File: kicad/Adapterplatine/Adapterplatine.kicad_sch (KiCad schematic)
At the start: 4 parts, among them X36A1 DE9_Pins, X40 Conn_01x02_Pin, X45 DE9_Pins, X52 Conn_01x05_Pin

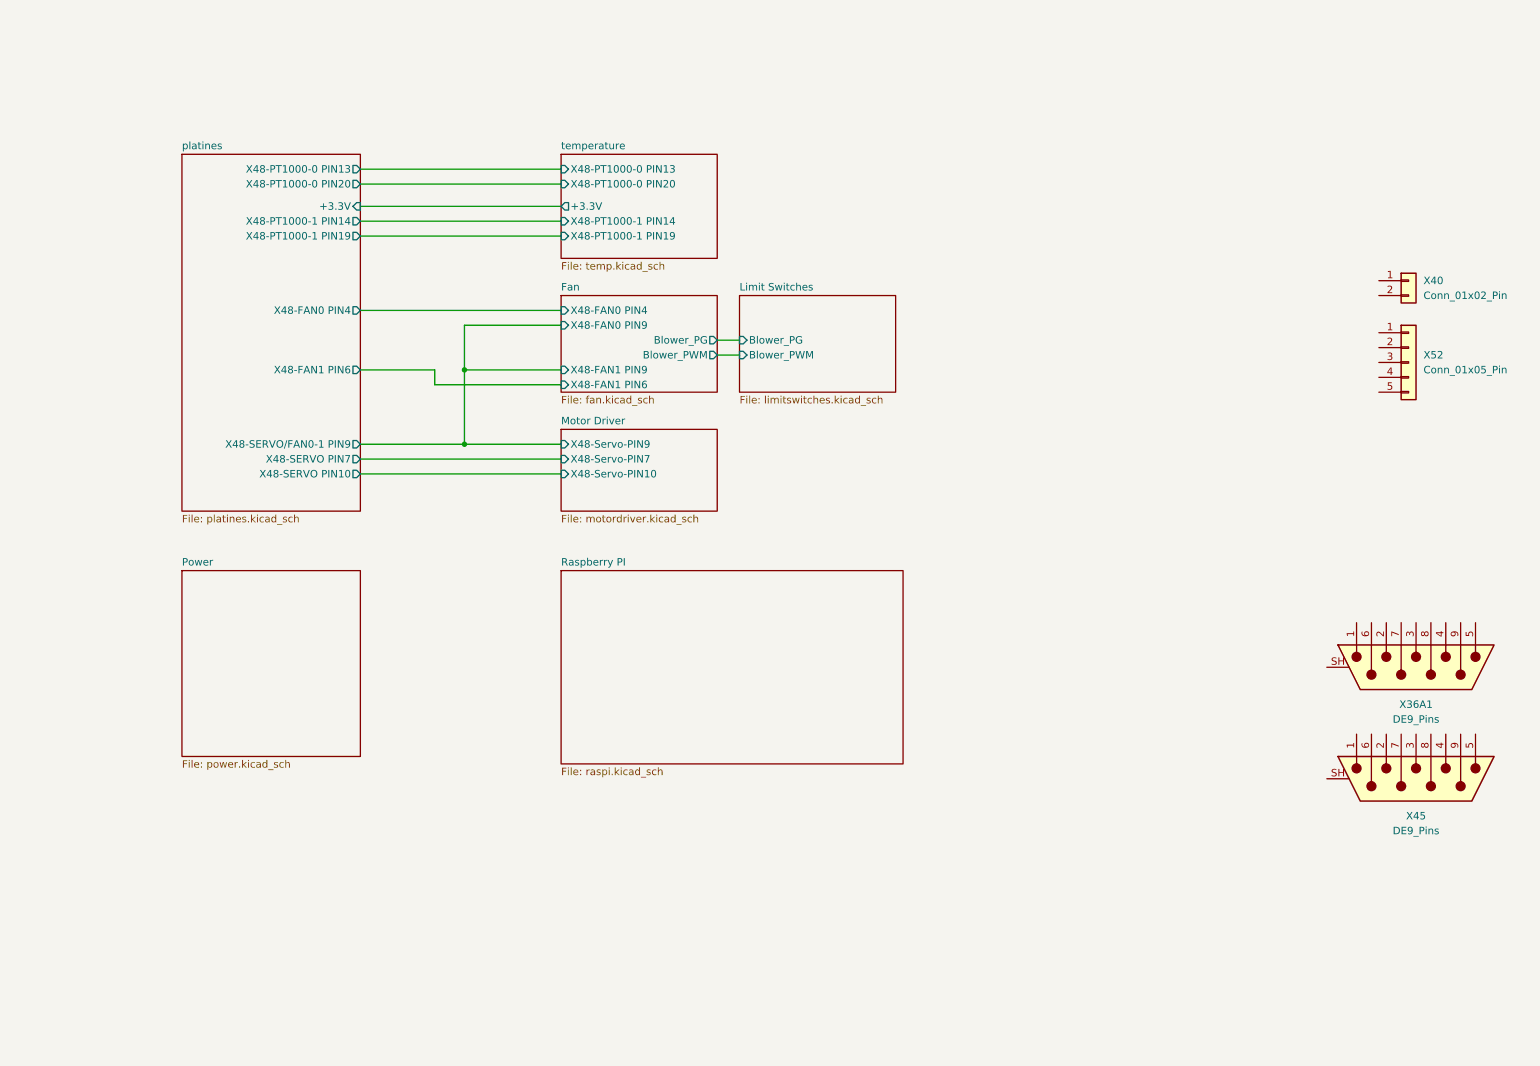
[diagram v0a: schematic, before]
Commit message: Abschlussbericht angefangen/ Adapterplatine ECR DCR
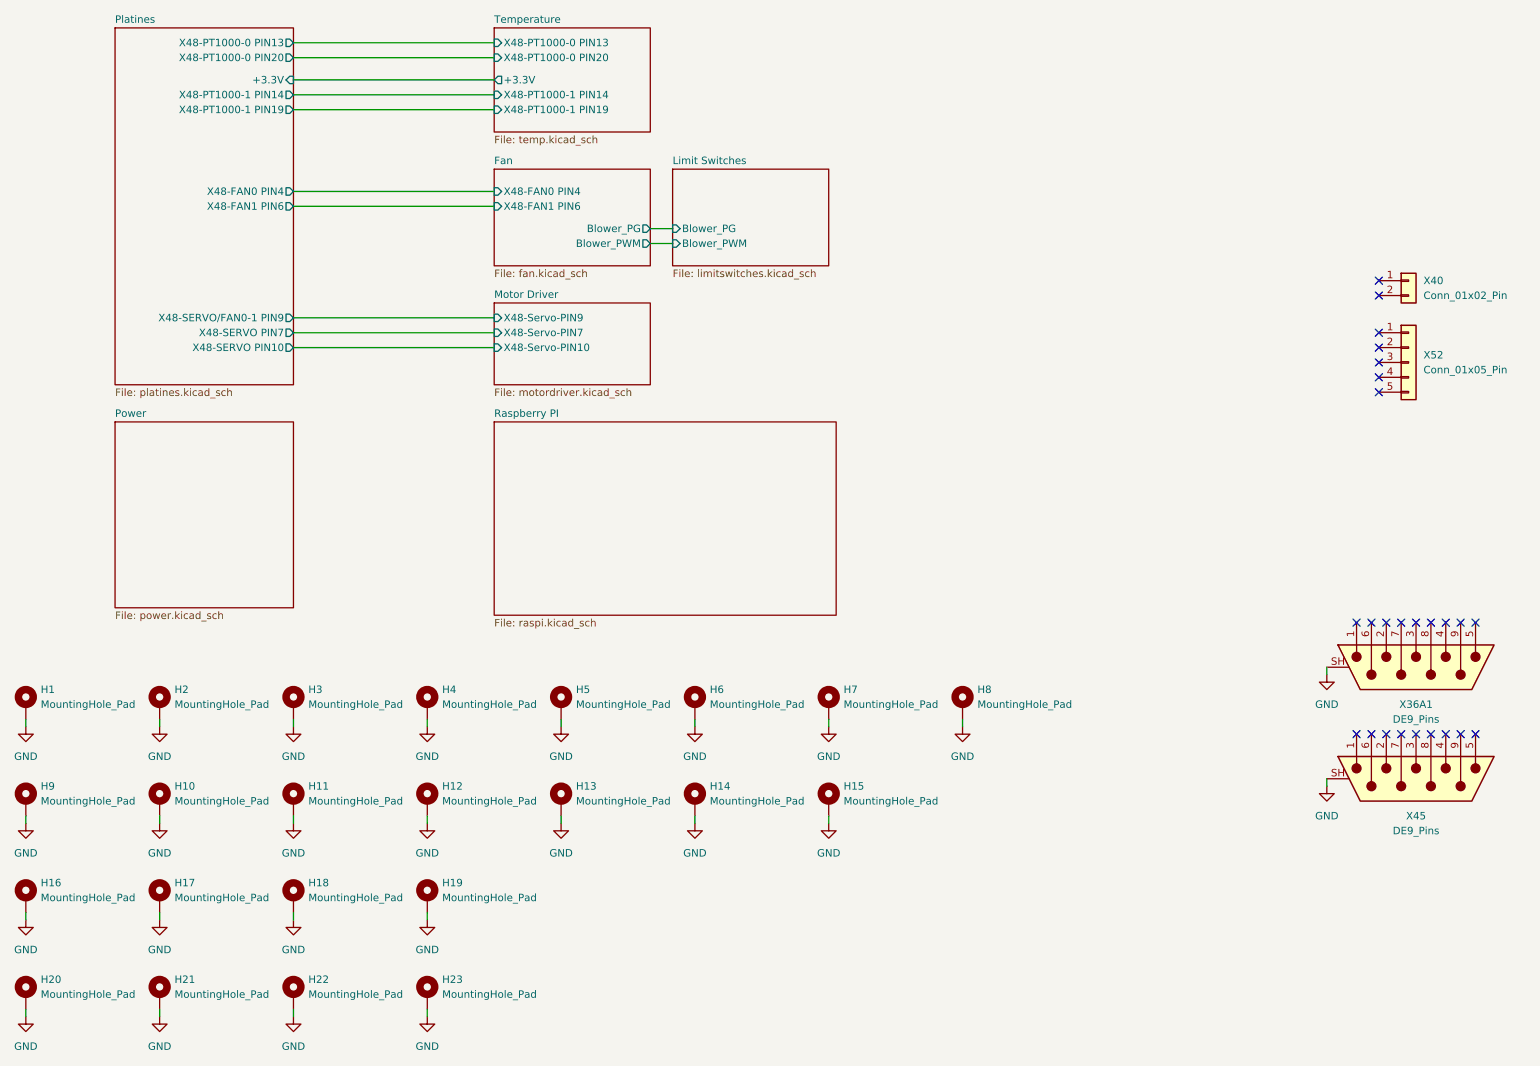
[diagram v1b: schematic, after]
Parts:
- added H1, H10, H11, H12, H13, H14, H15, H2, H3, H4, H5, H6, H7, H8, H9: MountingHole_Pad, MountingHole:MountingHole_3.5mm_Pad, symbol Mechanical:MountingHole_Pad
- added H16, H17, H18, H19, H20, H21, H22, H23: MountingHole_Pad, MountingHole:MountingHole_3.5mm_Pad_Via, symbol Mechanical:MountingHole_Pad
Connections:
- net GND: now reaches X45.SH (PAD)
- net GND: now also X36A1.SH (PAD), H1.1, H10.1, H11.1, H12.1, H13.1, H14.1, H15.1, H16.1, H17.1, H18.1, H19.1, H2.1, H20.1, H21.1, H22.1, H23.1, H3.1, H4.1, H5.1, H6.1, H7.1, H8.1, H9.1
- no-connect marks 0 -> 25
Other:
- sheet platines renamed Platines
- sheet temperature renamed Temperature
- sheet Fan ports: added none; removed X48-FAN0 PIN9, X48-FAN1 PIN9

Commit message: Adapterplatine Version 1.0
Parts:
- H16, H17, H18, H19, H20, H21, H22, H23: footprint MountingHole:MountingHole_3.5mm_Pad_Via -> Platines:MountingHole_3.5mm_Pad_Via_10mm_Aufbau
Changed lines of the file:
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@@
 			)
 		)
-		(property "Footprint" "MountingHole:MountingHole_3.5mm_Pad_Via"
+		(property "Footprint" "Platines:MountingHole_3.5mm_Pad_Via_10mm_Aufbau"
 			(at 40.64 186.69 0)
 			(hide yes)
@@
 			)
 		)
-		(property "Footprint" "MountingHole:MountingHole_3.5mm_Pad_Via"
+		(property "Footprint" "Platines:MountingHole_3.5mm_Pad_Via_10mm_Aufbau"
 			(at 63.5 186.69 0)
 			(hide yes)
@@
 			)
 		)
-		(property "Footprint" "MountingHole:MountingHole_3.5mm_Pad_Via"
+		(property "Footprint" "Platines:MountingHole_3.5mm_Pad_Via_10mm_Aufbau"
 			(at 86.36 170.18 0)
 			(hide yes)
@@
 			)
 		)
-		(property "Footprint" "MountingHole:MountingHole_3.5mm_Pad_Via"
+		(property "Footprint" "Platines:MountingHole_3.5mm_Pad_Via_10mm_Aufbau"
 			(at 17.78 170.18 0)
 			(hide yes)
@@
 			)
 		)
-		(property "Footprint" "MountingHole:MountingHole_3.5mm_Pad_Via"
+		(property "Footprint" "Platines:MountingHole_3.5mm_Pad_Via_10mm_Aufbau"
 			(at 17.78 186.69 0)
 			(hide yes)
@@
 			)
 		)
-		(property "Footprint" "MountingHole:MountingHole_3.5mm_Pad_Via"
+		(property "Footprint" "Platines:MountingHole_3.5mm_Pad_Via_10mm_Aufbau"
 			(at 40.64 170.18 0)
 			(hide yes)
@@
 			)
 		)
-		(property "Footprint" "MountingHole:MountingHole_3.5mm_Pad_Via"
+		(property "Footprint" "Platines:MountingHole_3.5mm_Pad_Via_10mm_Aufbau"
 			(at 86.36 186.69 0)
 			(hide yes)
@@
 			)
 		)
-		(property "Footprint" "MountingHole:MountingHole_3.5mm_Pad_Via"
+		(property "Footprint" "Platines:MountingHole_3.5mm_Pad_Via_10mm_Aufbau"
 			(at 63.5 170.18 0)
 			(hide yes)

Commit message: Adapterplatine Version 1.0 final
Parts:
- H1: Alternative (none) -> -; Hersteller (none) -> -; Herstellerbezeichnung (none) -> -
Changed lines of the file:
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@@
 			)
 		)
-		(property "Hersteller" ""
+		(property "Hersteller" "-"
 			(at 17.78 137.16 0)
 			(hide yes)
@@
 			)
 		)
-		(property "Herstellerbezeichnung" ""
+		(property "Herstellerbezeichnung" "-"
 			(at 17.78 137.16 0)
 			(hide yes)
@@
 			)
 		)
-		(property "Alternative" ""
+		(property "Alternative" "-"
 			(at 17.78 137.16 0)
 			(hide yes)
